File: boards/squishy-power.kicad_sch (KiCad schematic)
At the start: 92 parts, among them U1 THVD1452DGSR, U10 THVD1452DGSR, U11 FXL4TD245BQX, U13 THVD1452DGSR, U15 THVD1452DGSR, U16 FXL4TD245BQX, U17 THVD1452DGSR, U18 THVD1452DGSR, U2 FXL4TD245BQX, U20 FXL4TD245BQX, U21 THVD1452DGSR, U22 THVD1452DGSR, U23 FXL4TD245BQX, U24 THVD1452DGSR, U25 THVD1452DGSR, U26 W25N01GVZEIG, U27 FXL4TD245BQX, U28 THVD1452DGSR, U29 THVD1452DGSR, U3 TLV755533PDRVR, U30 FXL4TD245BQX, U31 THVD1452DGSR, U32 THVD1452DGSR, U33 FXL4TD245BQX, U34 THVD1452DGSR, U4 THVD1452DGSR, U5 TLV73312PQDRVRQ1, U6 THVD1452DGSR, U7 LP5910-1.8DRVR, U8 FXL4TD245BQX, U9 THVD1452DGSR

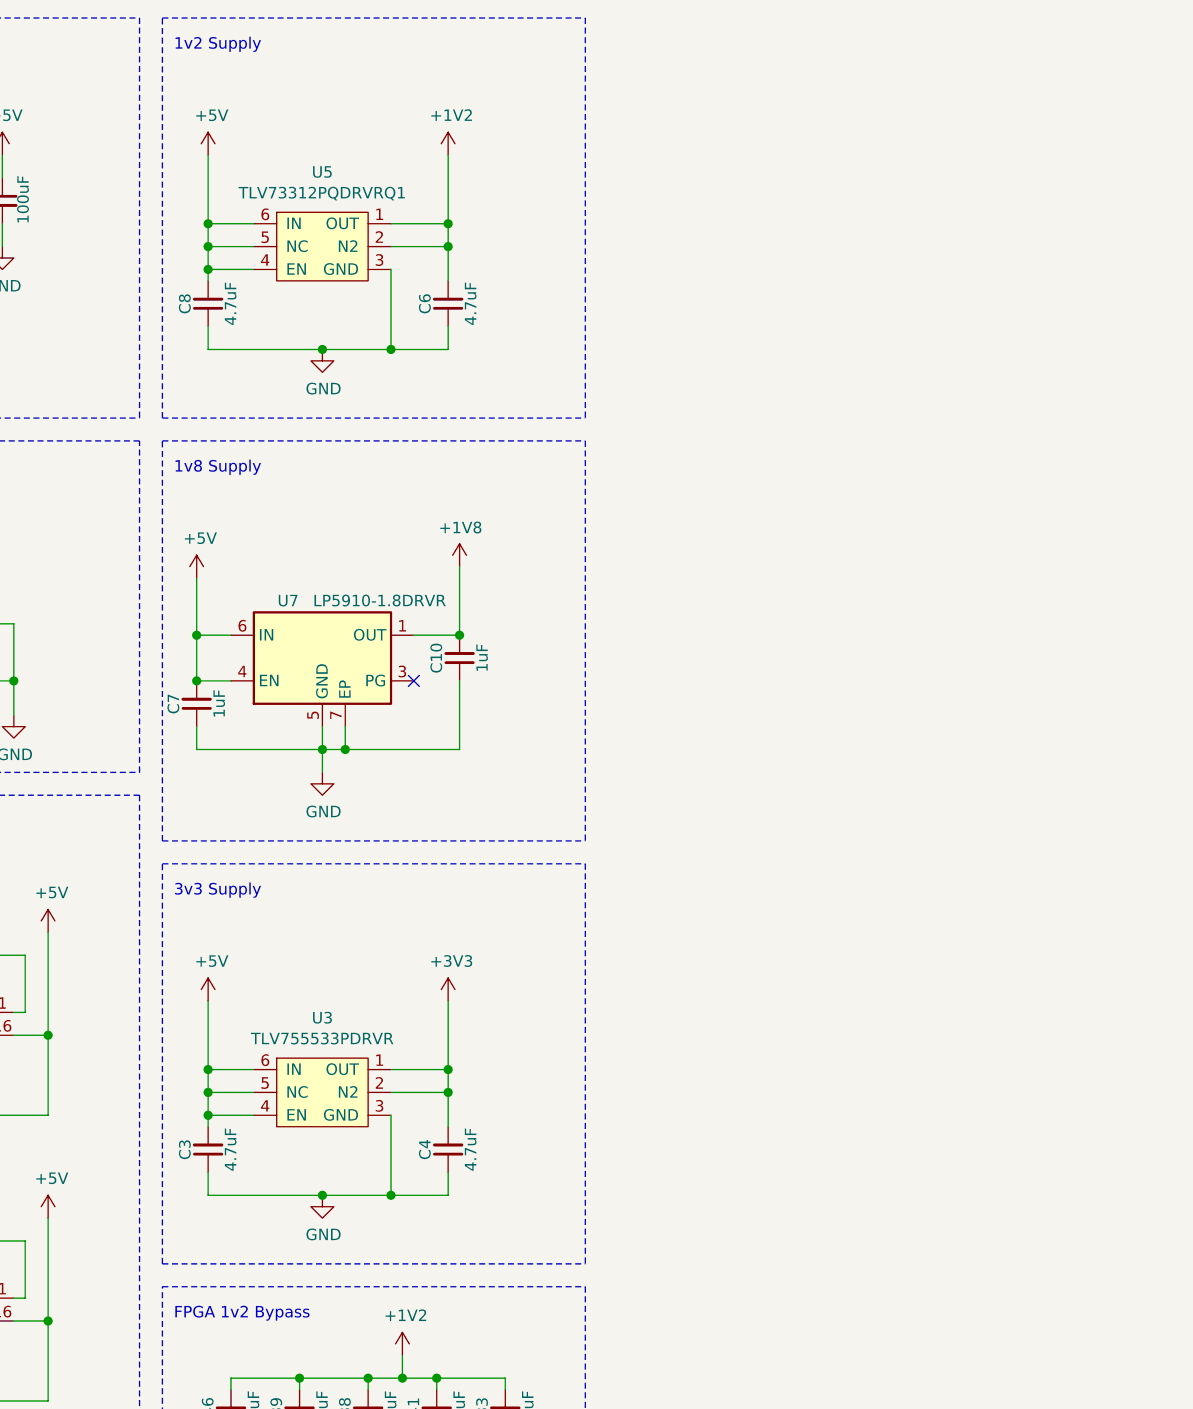
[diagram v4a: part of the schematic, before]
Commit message: hardware: added reset gen for power sequencing
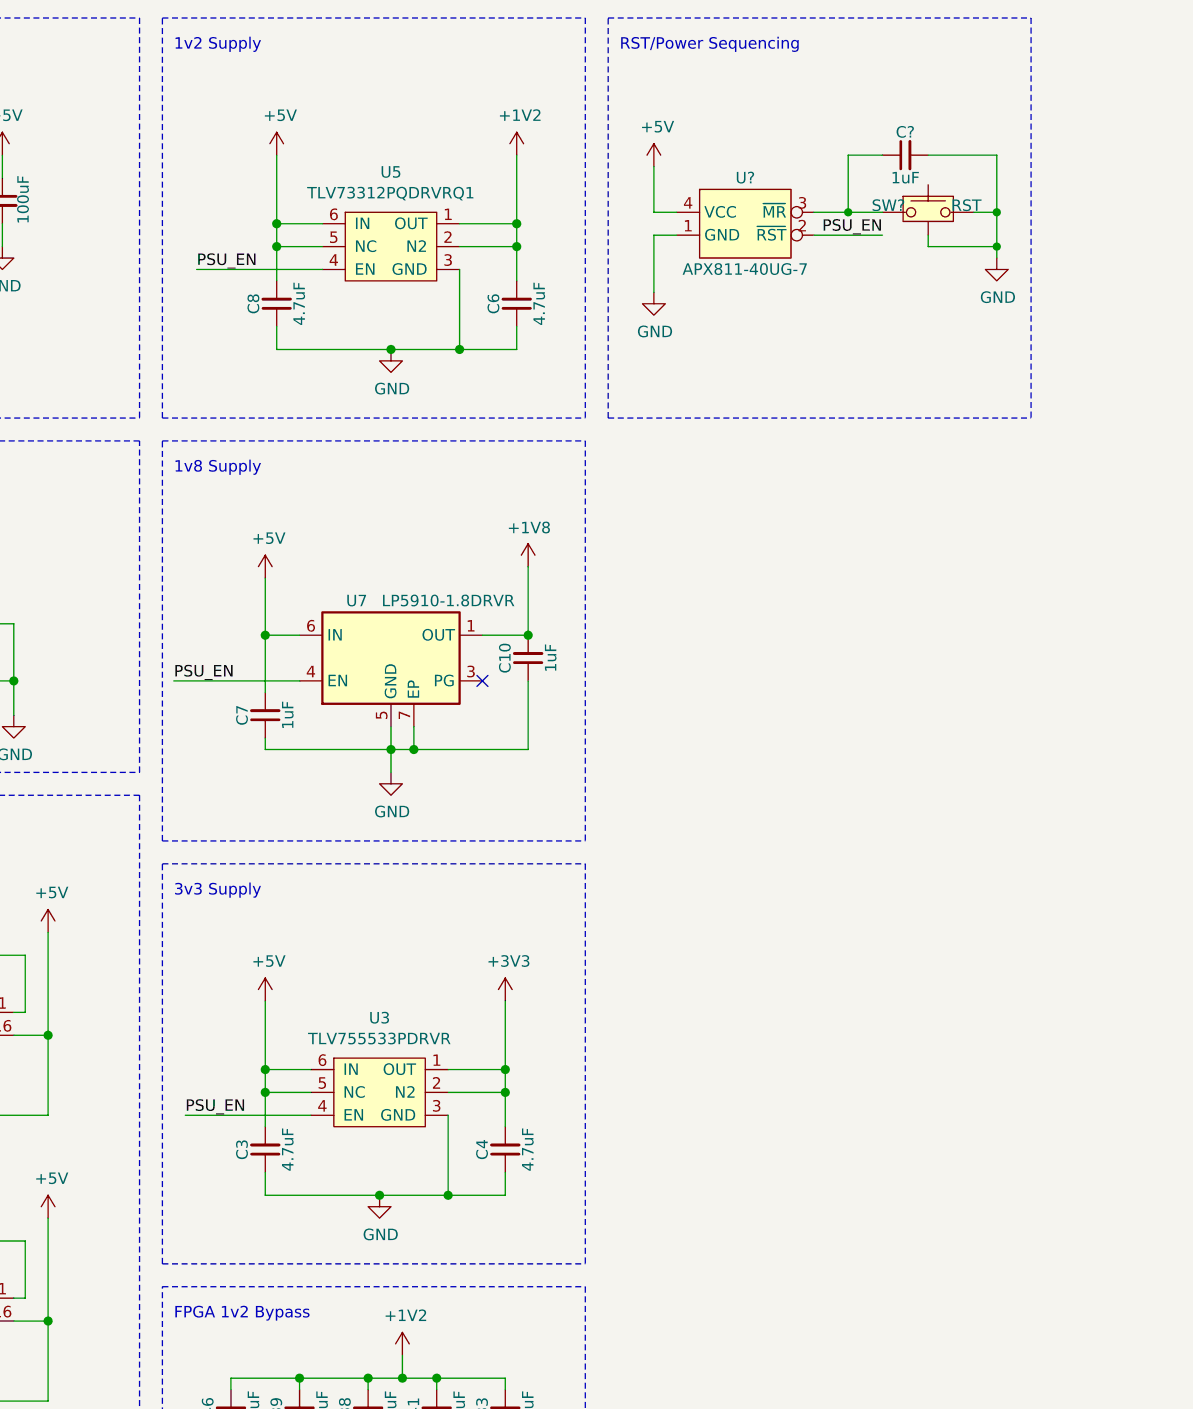
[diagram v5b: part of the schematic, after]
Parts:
- added C?: 1uF, Capacitor_SMD:C_0603_1608Metric, symbol Device:C_Small
- added SW?: RST, lethalbit:SW_Tactile_SPST_Angled_TC-1109DE, symbol lethalbit:SW_Push_Shield
- added U?: APX811-40UG-7, Package_TO_SOT_SMD:SOT-143, symbol lethalbit:APX811-40UG-7
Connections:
- net +5V: now also U?.4 (VCC); no longer U3.4 (EN), U5.4 (EN), U7.4 (EN)
- net GND: now also C?.2, SW?.2, SW?.3, U?.1 (GND)
- new net: C?.1, SW?.1, U?.3 (~{MR})
- new net PSU_EN: U3.4 (EN), U5.4 (EN), U7.4 (EN), U?.2 (~{RST})
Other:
- note added: "RST/Power Sequencing"
- moved on the sheet: C10, C3, C4, C6, C7, C8, U3, U5, U7

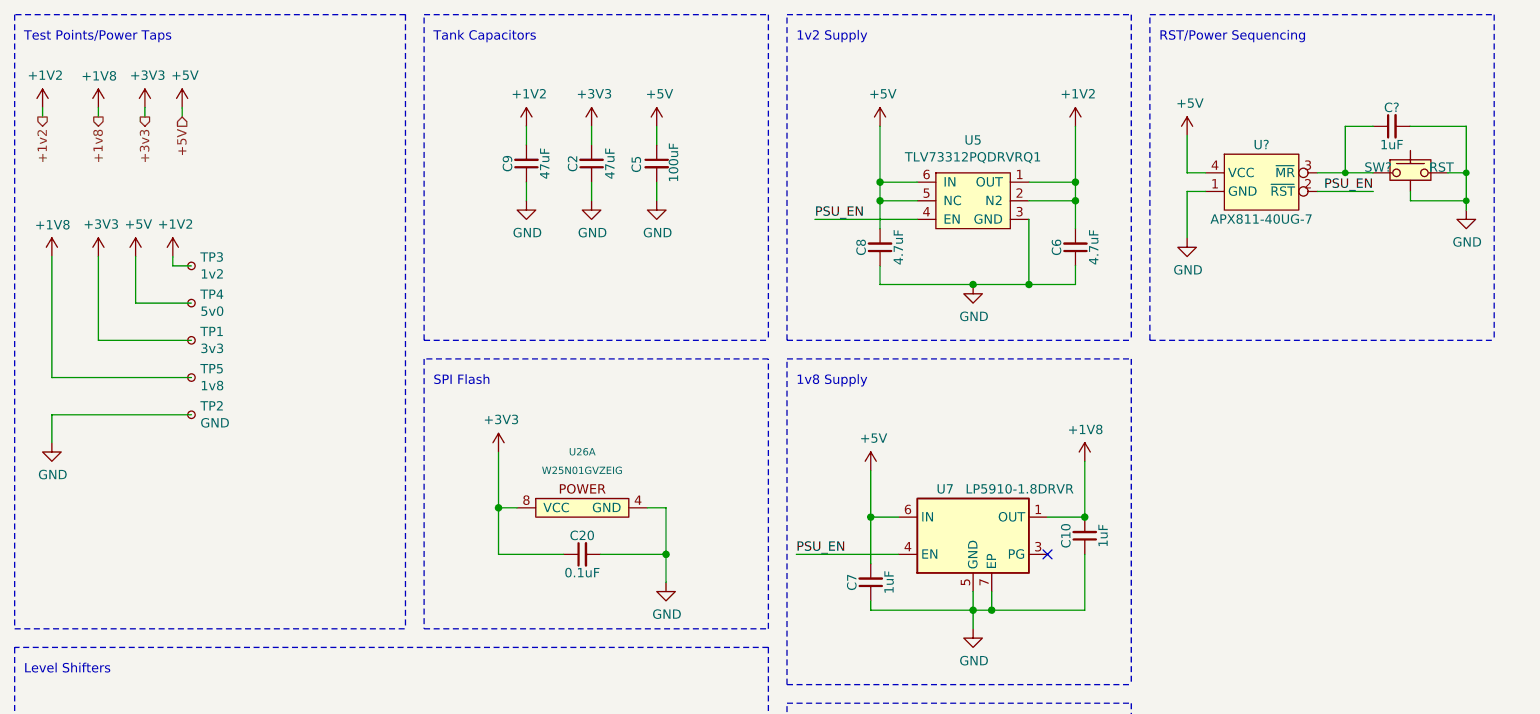
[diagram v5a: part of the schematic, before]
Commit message: hardware: added additional ground points
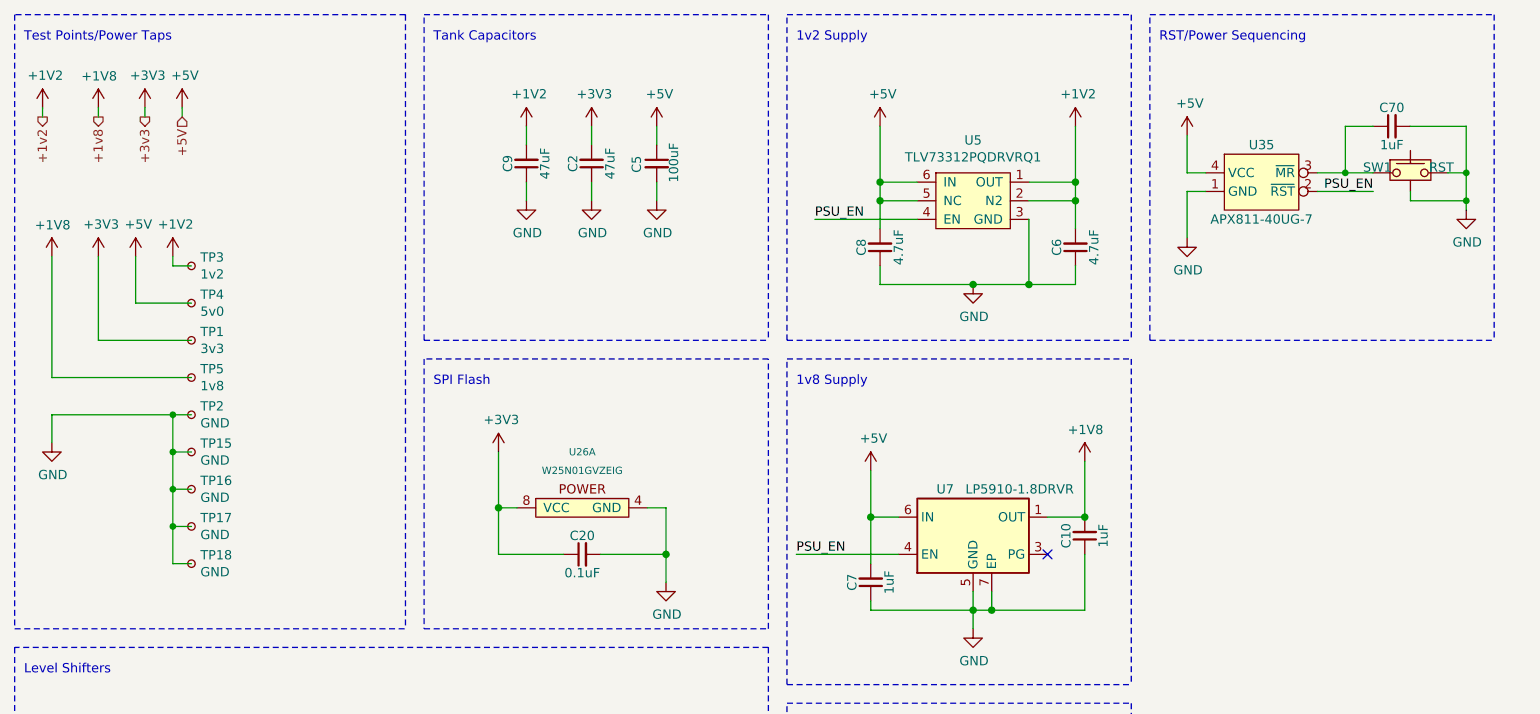
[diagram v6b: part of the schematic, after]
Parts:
- added TP15, TP16, TP17, TP18: GND, TestPoint:TestPoint_Pad_D1.0mm, symbol Connector:TestPoint_Small
- gave numbers to parts that had none: 3
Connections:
- net GND: now also TP15.1, TP16.1, TP17.1, TP18.1
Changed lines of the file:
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@@
   (junction (at 25.4 233.68) (diameter 1.016) (color 0 0 0 0))
   (junction (at 25.4 261.62) (diameter 1.016) (color 0 0 0 0))
+  (junction (at 35.56 68.58) (diameter 0) (color 0 0 0 0))
+  (junction (at 35.56 73.66) (diameter 0) (color 0 0 0 0))
+  (junction (at 35.56 78.74) (diameter 0) (color 0 0 0 0))
+  (junction (at 35.56 83.82) (diameter 0) (color 0 0 0 0))
   (junction (at 38.1 118.11) (diameter 1.016) (color 0 0 0 0))
   (junction (at 38.1 149.86) (diameter 1.016) (color 0 0 0 0))
@@
     (stroke (width 0) (type solid) (color 0 0 0 0))
   )
-  (wire (pts (xy 19.05 68.58) (xy 38.1 68.58))
+  (wire (pts (xy 19.05 68.58) (xy 35.56 68.58))
     (stroke (width 0) (type solid) (color 0 0 0 0))
   )
@@
     (stroke (width 0) (type solid) (color 0 0 0 0))
   )
+  (wire (pts (xy 35.56 68.58) (xy 35.56 73.66))
+    (stroke (width 0) (type default) (color 0 0 0 0))
+  )
+  (wire (pts (xy 35.56 68.58) (xy 38.1 68.58))
+    (stroke (width 0) (type solid) (color 0 0 0 0))
+  )
+  (wire (pts (xy 35.56 73.66) (xy 35.56 78.74))
+    (stroke (width 0) (type default) (color 0 0 0 0))
+  )
+  (wire (pts (xy 35.56 73.66) (xy 38.1 73.66))
+    (stroke (width 0) (type default) (color 0 0 0 0))
+  )
+  (wire (pts (xy 35.56 78.74) (xy 35.56 83.82))
+    (stroke (width 0) (type default) (color 0 0 0 0))
+  )
+  (wire (pts (xy 35.56 78.74) (xy 38.1 78.74))
+    (stroke (width 0) (type default) (color 0 0 0 0))
+  )
+  (wire (pts (xy 35.56 83.82) (xy 35.56 88.9))
+    (stroke (width 0) (type default) (color 0 0 0 0))
+  )
+  (wire (pts (xy 35.56 83.82) (xy 38.1 83.82))
+    (stroke (width 0) (type default) (color 0 0 0 0))
+  )
+  (wire (pts (xy 35.56 88.9) (xy 38.1 88.9))
+    (stroke (width 0) (type default) (color 0 0 0 0))
+  )
   (wire (pts (xy 35.56 135.89) (xy 45.72 135.89))
     (stroke (width 0) (type solid) (color 0 0 0 0))
@@
     (pin "1")
   )
+  (symbol (lib_id "Connector:TestPoint_Small") (at 38.1 73.66 0) (unit 1)
+    (in_bom yes) (on_board yes)
+    (property "Reference" "TP15" (id 0) (at 39.3192 72.4916 0)
+      (effects (font (size 1.27 1.27)) (justify left))
+    )
+    (property "Value" "GND" (id 1) (at 39.3192 74.803 0)
+      (effects (font (size 1.27 1.27)) (justify left))
+    )
+    (property "Footprint" "TestPoint:TestPoint_Pad_D1.0mm" (id 2) (at 43.18 73.66 0)
+      (effects (font (size 1.27 1.27)) hide)
+    )
+    (property "Datasheet" "~" (id 3) (at 43.18 73.66 0)
+      (effects (font (size 1.27 1.27)) hide)
+    )
+    (property "MFR" "N/A" (id 4) (at 38.1 73.66 0)
+      (effects (font (size 1.27 1.27)) hide)
+    )
+    (property "MPN" "N/A" (id 5) (at 38.1 73.66 0)
+      (effects (font (size 1.27 1.27)) hide)
+    )
+    (pin "1")
+  )
+  (symbol (lib_id "Connector:TestPoint_Small") (at 38.1 78.74 0) (unit 1)
+    (in_bom yes) (on_board yes)
+    (property "Reference" "TP16" (id 0) (at 39.3192 77.5716 0)
+      (effects (font (size 1.27 1.27)) (justify left))
+    )
+    (property "Value" "GND" (id 1) (at 39.3192 79.883 0)
+      (effects (font (size 1.27 1.27)) (justify left))
+    )
+    (property "Footprint" "TestPoint:TestPoint_Pad_D1.0mm" (id 2) (at 43.18 78.74 0)
+      (effects (font (size 1.27 1.27)) hide)
+    )
+    (property "Datasheet" "~" (id 3) (at 43.18 78.74 0)
+      (effects (font (size 1.27 1.27)) hide)
+    )
+    (property "MFR" "N/A" (id 4) (at 38.1 78.74 0)
+      (effects (font (size 1.27 1.27)) hide)
+    )
+    (property "MPN" "N/A" (id 5) (at 38.1 78.74 0)
+      (effects (font (size 1.27 1.27)) hide)
+    )
+    (pin "1")
+  )
+  (symbol (lib_id "Connector:TestPoint_Small") (at 38.1 83.82 0) (unit 1)
+    (in_bom yes) (on_board yes)
+    (property "Reference" "TP17" (id 0) (at 39.3192 82.6516 0)
+      (effects (font (size 1.27 1.27)) (justify left))
+    )
+    (property "Value" "GND" (id 1) (at 39.3192 84.963 0)
+      (effects (font (size 1.27 1.27)) (justify left))
+    )
+    (property "Footprint" "TestPoint:TestPoint_Pad_D1.0mm" (id 2) (at 43.18 83.82 0)
+      (effects (font (size 1.27 1.27)) hide)
+    )
+    (property "Datasheet" "~" (id 3) (at 43.18 83.82 0)
+      (effects (font (size 1.27 1.27)) hide)
+    )
+    (property "MFR" "N/A" (id 4) (at 38.1 83.82 0)
+      (effects (font (size 1.27 1.27)) hide)
+    )
+    (property "MPN" "N/A" (id 5) (at 38.1 83.82 0)
+      (effects (font (size 1.27 1.27)) hide)
+    )
+    (pin "1")
+  )
+  (symbol (lib_id "Connector:TestPoint_Small") (at 38.1 88.9 0) (unit 1)
+    (in_bom yes) (on_board yes)
+    (property "Reference" "TP18" (id 0) (at 39.3192 87.7316 0)
+      (effects (font (size 1.27 1.27)) (justify left))
+    )
+    (property "Value" "GND" (id 1) (at 39.3192 90.043 0)
+      (effects (font (size 1.27 1.27)) (justify left))
+    )
+    (property "Footprint" "TestPoint:TestPoint_Pad_D1.0mm" (id 2) (at 43.18 88.9 0)
+      (effects (font (size 1.27 1.27)) hide)
+    )
+    (property "Datasheet" "~" (id 3) (at 43.18 88.9 0)
+      (effects (font (size 1.27 1.27)) hide)
+    )
+    (property "MFR" "N/A" (id 4) (at 38.1 88.9 0)
+      (effects (font (size 1.27 1.27)) hide)
+    )
+    (property "MPN" "N/A" (id 5) (at 38.1 88.9 0)
+      (effects (font (size 1.27 1.27)) hide)
+    )
+    (pin "1")
+  )
   (symbol (lib_id "power:+1V2") (at 17.78 26.67 0) (unit 1)
     (in_bom yes) (on_board yes)
@@
   (symbol (lib_id "power:+5V") (at 173.99 30.48 0) (unit 1)
     (in_bom yes) (on_board yes)
-    (property "Reference" "#PWR?" (id 0) (at 173.99 34.29 0)
+    (property "Reference" "#PWR0241" (id 0) (at 173.99 34.29 0)
       (effects (font (size 1.27 1.27)) hide)
     )
@@
   (symbol (lib_id "power:GND") (at 173.99 44.45 0) (unit 1)
     (in_bom yes) (on_board yes)
-    (property "Reference" "#PWR?" (id 0) (at 173.99 50.8 0)
+    (property "Reference" "#PWR0242" (id 0) (at 173.99 50.8 0)
       (effects (font (size 1.27 1.27)) hide)
     )
@@
   (symbol (lib_id "power:GND") (at 212.09 40.64 0) (unit 1)
     (in_bom yes) (on_board yes)
-    (property "Reference" "#PWR?" (id 0) (at 212.09 46.99 0)
+    (property "Reference" "#PWR0240" (id 0) (at 212.09 46.99 0)
       (effects (font (size 1.27 1.27)) hide)
     )
@@
   (symbol (lib_id "Device:C_Small") (at 201.93 29.21 90) (unit 1)
     (in_bom yes) (on_board yes)
-    (property "Reference" "C?" (id 0) (at 201.93 26.67 90))
+    (property "Reference" "C70" (id 0) (at 201.93 26.67 90))
     (property "Value" "1uF" (id 1) (at 201.93 31.75 90))
     (property "Footprint" "Capacitor_SMD:C_0603_1608Metric" (id 2) (at 201.93 29.21 0)
@@
   (symbol (lib_id "lethalbit:SW_Push_Shield") (at 204.47 35.56 0) (unit 1)
     (in_bom yes) (on_board yes)
-    (property "Reference" "SW?" (id 0) (at 201.93 35.56 0)
+    (property "Reference" "SW1" (id 0) (at 201.93 35.56 0)
       (effects (font (size 1.27 1.27)) (justify right bottom))
     )
@@
   (symbol (lib_id "lethalbit:APX811-40UG-7") (at 184.15 36.83 0) (unit 1)
     (in_bom yes) (on_board yes)
-    (property "Reference" "U?" (id 0) (at 184.15 31.75 0))
+    (property "Reference" "U35" (id 0) (at 184.15 31.75 0))
     (property "Value" "APX811-40UG-7" (id 1) (at 184.15 41.91 0))
     (property "Footprint" "Package_TO_SOT_SMD:SOT-143" (id 2) (at 184.15 44.45 0)

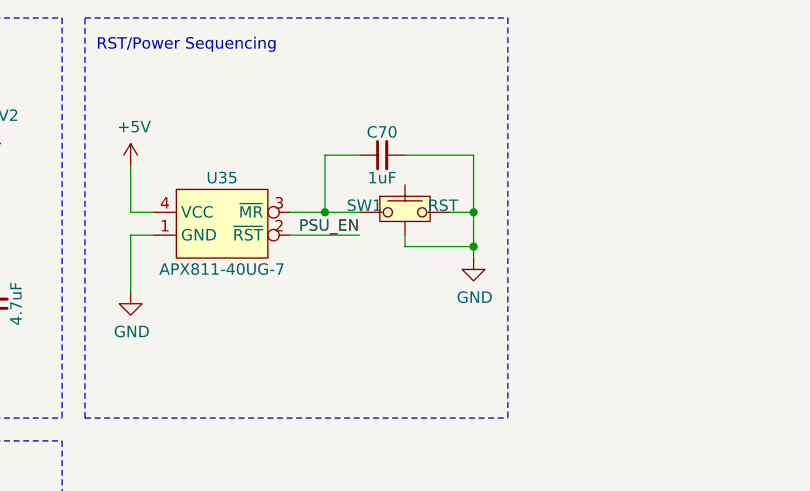
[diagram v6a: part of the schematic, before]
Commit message: hardware: fipped the reset button pins around to make more sense and placed the reset button
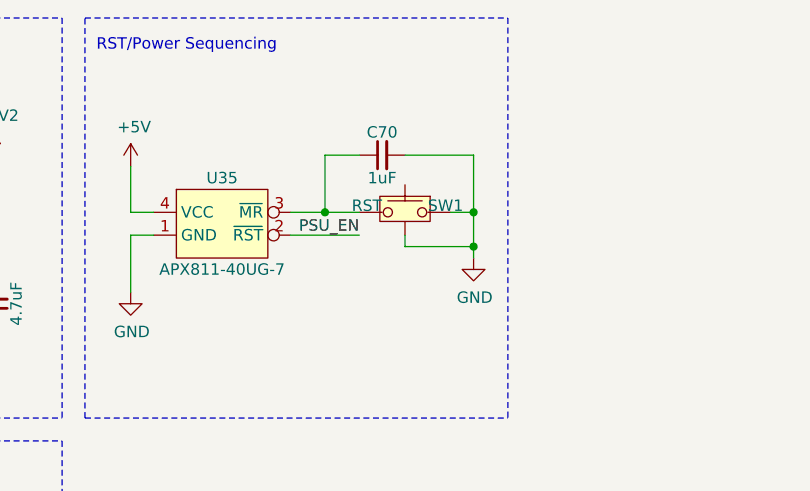
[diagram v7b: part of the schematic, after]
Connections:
- net GND: now also SW1.1; no longer SW1.2
- net at C70.1, U35.3 (~{MR}): now also SW1.2; no longer SW1.1
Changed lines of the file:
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@@
     (pin "2")
   )
-  (symbol (lib_id "lethalbit:SW_Push_Shield") (at 204.47 35.56 0) (unit 1)
+  (symbol (lib_id "lethalbit:SW_Push_Shield") (at 204.47 35.56 0) (mirror y) (unit 1)
     (in_bom yes) (on_board yes)
-    (property "Reference" "SW1" (id 0) (at 201.93 35.56 0)
+    (property "Reference" "SW1" (id 0) (at 207.01 35.56 0)
       (effects (font (size 1.27 1.27)) (justify right bottom))
     )
-    (property "Value" "RST" (id 1) (at 207.01 35.56 0)
+    (property "Value" "RST" (id 1) (at 201.93 35.56 0)
       (effects (font (size 1.27 1.27)) (justify left bottom))
     )
